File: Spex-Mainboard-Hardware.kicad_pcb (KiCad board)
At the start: 4 copper layers, 100 x 80 mm, 141 parts, among them K1 G5LE_1A4_DC3, K2 G5LE_1A4_DC3, P1 USB_OTG, P10 CONN_01X02, P11 CONN_01X02, P12 CONN_01X02, P2 SWD Header, P3 CONN_01X04, P4 CONN_01X04, P5 CONN_01X04, P6 CONN_01X04, P7 CONN_01X02, P8 CONN_01X02, P9 CONN_01X02, Q1 2N7002K, Q101 MOS_N_numbered, Q104 MOS_N_numbered, Q105 Si3407DV, Q106 Q_PNP_BEC, Q2 2N7002K, Q3 BSS215PH6327, Q4 Si5468DC, Q5 Si5468DC, Q6 Si5468DC, SW1 SW_PUSH, U1 MKL04Z32VLC4, U10 LM4030, U105 TPS563200, U108 TPS563200, U11 MCP2551-I/SN, U12 ST1480ABDR, U13 SCHA4B0419, U14 AT45DB641E, U2 NUP2201MR6, U3 MK20DX256VLH7, U4 NUP2201MR6, U5 NUP2201MR6, U6 MMQA6V2T1G, U7 MCP9808T, U8 BME280, U9 LSM9DS1, Y1 Crystal

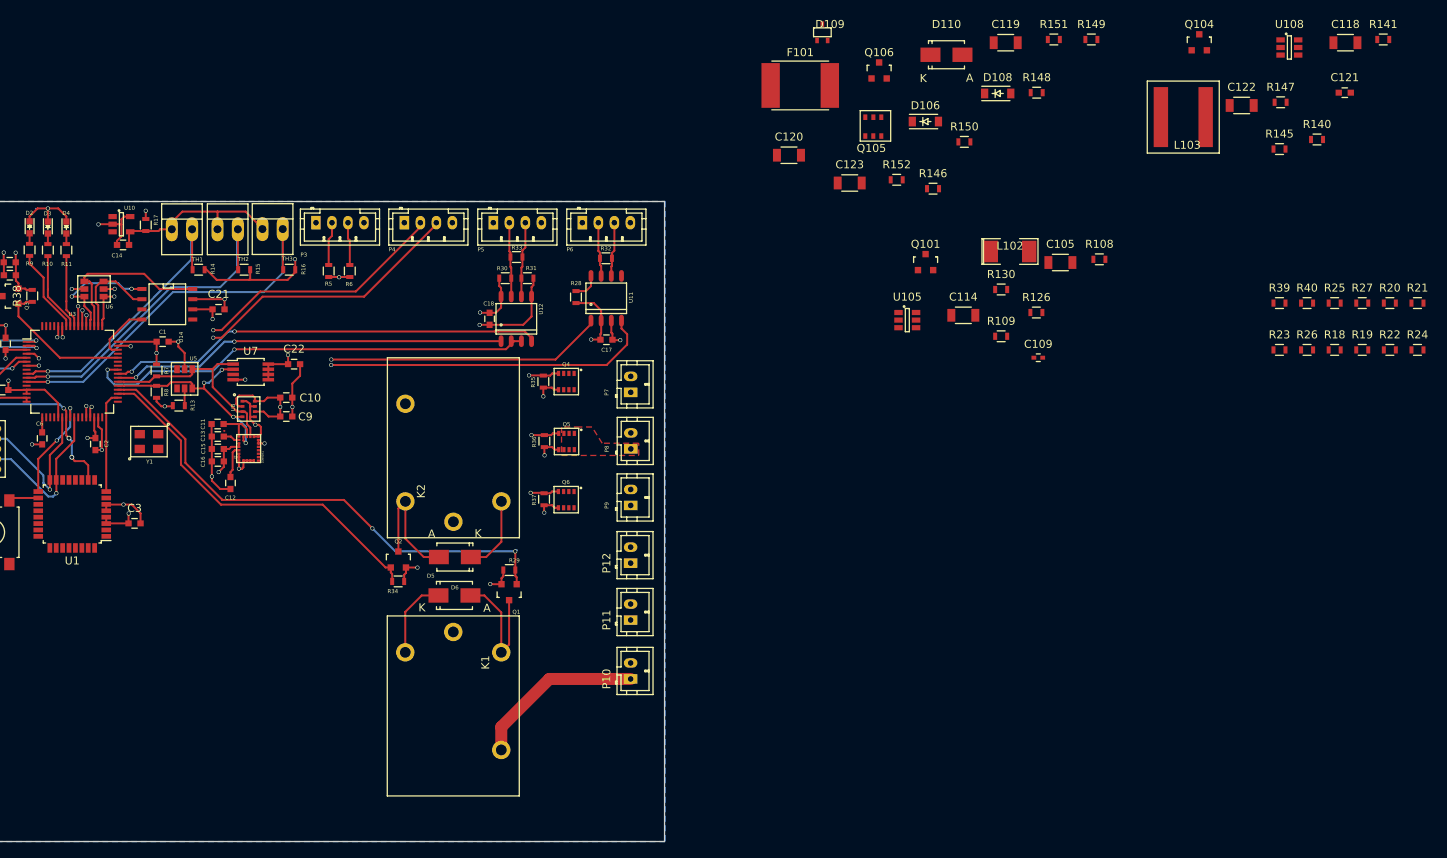
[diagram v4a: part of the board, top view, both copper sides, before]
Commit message: Added powerz
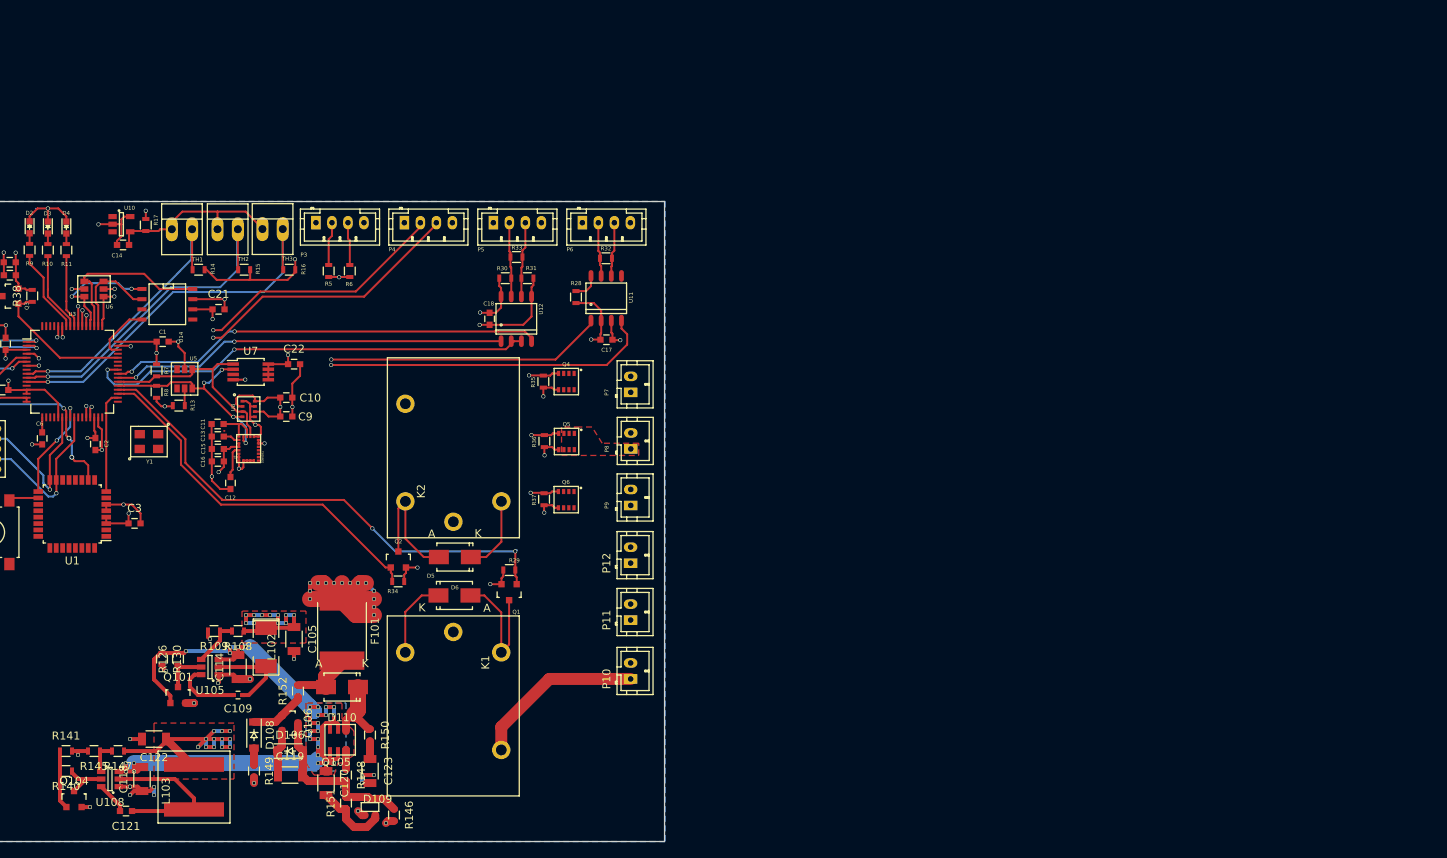
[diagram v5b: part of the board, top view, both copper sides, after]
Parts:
- removed R18, R19, R20, R21, R22, R23, R24, R25, R26, R27, R39, R40: R, Resistors_SMD:R_0603
- moved R141 187.1 mm to (109.0, 119.5)
- moved C121 176.8 mm to (116.5, 127.0), turned to 180 degrees
- moved C118 176.4 mm to (118.5, 123.0), turned to 90 degrees
- moved R140 175.2 mm to (109.0, 122.0), turned to 180 degrees
- moved U108 173.5 mm to (114.5, 123.0), turned to 180 degrees
- moved Q104 169.5 mm to (110.0, 125.5)
- moved R147 166.4 mm to (115.5, 119.5), turned to 180 degrees
- moved R145 166.2 mm to (112.5, 119.5), turned to 180 degrees
- moved C122 157.3 mm to (120.0, 118.0), turned to 180 degrees
- moved L103 149.3 mm to (125.0, 124.0), turned to 270 degrees
- moved R149 139.0 mm to (132.5, 122.0), turned to 270 degrees
- moved R151 130.1 mm to (144.0, 126.0), turned to 90 degrees
- moved C119 128.0 mm to (137.0, 122.5)
- moved D108 122.8 mm to (132.5, 117.5), turned to 270 degrees
- moved R148 121.4 mm to (144.0, 122.5), turned to 270 degrees
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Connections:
- C105 pad 1: /Power Distribution/12Vto3v3.sch/Vout -> +3V3
- C122 pad 1: /Power Distribution/12Vto5V.sch/Vout -> +5V
- C123 pad 2: /Power Distribution/protection.sch/GND -> GND
- D109 pad 1: /Power Distribution/protection.sch/GND -> GND
- D110 pad 1: Net-(D110-Pad1) -> Net-(C119-Pad1)
- D110 pad 2: Net-(C119-Pad1) -> Net-(D110-Pad2)
- F101 pad 1: /Power Distribution/protection.sch/Vin -> VBatt
- F101 pad 2: Net-(D110-Pad1) -> Net-(D110-Pad2)
- L102 pad 1: /Power Distribution/12Vto3v3.sch/Vout -> +3V3
- L103 pad 1: /Power Distribution/12Vto5V.sch/Vout -> +5V
- P2 pad 10: /RESET_b -> (no net)
- P2 pad 6: Net-(P2-Pad6) -> (no net)
- P2 pad 7: Net-(P2-Pad7) -> (no net)
- P2 pad 8: Net-(P2-Pad8) -> (no net)
- P2 pad 9: Net-(P2-Pad9) -> (no net)
- P9 pad 2: Vbus -> (no net)
- Q3 pad 3: Net-(Q3-Pad3) -> (no net)
- R108 pad 1: /Power Distribution/12Vto3v3.sch/Vout -> +3V3
- R146 pad 2: /Power Distribution/protection.sch/GND -> GND
- R147 pad 1: /Power Distribution/12Vto5V.sch/Vout -> +5V
- R149 pad 2: /Power Distribution/protection.sch/GND -> GND
- R152 pad 2: Net-(D110-Pad1) -> Net-(D110-Pad2)
- U1 pad 1: Net-(U1-Pad1) -> (no net)
- U1 pad 11: Net-(U1-Pad11) -> (no net)
- U1 pad 12: Net-(U1-Pad12) -> (no net)
- U1 pad 13: Net-(U1-Pad13) -> (no net)
- U1 pad 14: Net-(U1-Pad14) -> (no net)
- U1 pad 19: Net-(U1-Pad19) -> (no net)
- U1 pad 2: Net-(U1-Pad2) -> (no net)
- U1 pad 20: Net-(U1-Pad20) -> (no net)
- U1 pad 21: Net-(U1-Pad21) -> (no net)
- U1 pad 22: Net-(U1-Pad22) -> (no net)
- U1 pad 23: Net-(U1-Pad23) -> (no net)
- U1 pad 24: Net-(U1-Pad24) -> (no net)
- U1 pad 25: /PTB5 -> (no net)
- U1 pad 26: Net-(U1-Pad26) -> (no net)
- U1 pad 27: Net-(U1-Pad27) -> (no net)
- U1 pad 28: Net-(U1-Pad28) -> (no net)
- U1 pad 29: Net-(U1-Pad29) -> (no net)
- U1 pad 30: Net-(U1-Pad30) -> (no net)
- U1 pad 31: Net-(U1-Pad31) -> (no net)
- U1 pad 32: Net-(U1-Pad32) -> (no net)
- U1 pad 7: Net-(U1-Pad7) -> (no net)
- U1 pad 9: Net-(U1-Pad9) -> (no net)
- U10 pad 1: Net-(U10-Pad1) -> (no net)
- U10 pad 3: Net-(U10-Pad3) -> (no net)
- U11 pad 5: Net-(U11-Pad5) -> (no net)
- U14 pad 3: Net-(U14-Pad3) -> (no net)
- U14 pad 5: Net-(U14-Pad5) -> (no net)
- U2 pad 3: Net-(U2-Pad3) -> (no net)
- U2 pad 4: Net-(U2-Pad4) -> (no net)
- U3 pad 12: Net-(U3-Pad12) -> (no net)
- U3 pad 18: Net-(U3-Pad18) -> (no net)
- U3 pad 19: Net-(U3-Pad19) -> (no net)
- U3 pad 20: Net-(U3-Pad20) -> (no net)
- U3 pad 26: Net-(U3-Pad26) -> (no net)
- U3 pad 27: Net-(U3-Pad27) -> (no net)
- U3 pad 42: Net-(U3-Pad42) -> (no net)
- U3 pad 43: Net-(U3-Pad43) -> (no net)
- U3 pad 45: SD_Detect -> (no net)
- U3 pad 61: Net-(U3-Pad61) -> (no net)
- U3 pad 62: Net-(U3-Pad62) -> (no net)
- U3 pad 63: Net-(U3-Pad63) -> (no net)
- U3 pad 64: Net-(U3-Pad64) -> (no net)
- U3 pad 8: Net-(U3-Pad8) -> (no net)
- U4 pad 3: Net-(U4-Pad3) -> (no net)
- U4 pad 4: Net-(U4-Pad4) -> (no net)
- U5 pad 3: Net-(U5-Pad3) -> (no net)
- U5 pad 4: Net-(U5-Pad4) -> (no net)
- U7 pad 3: /HAB Sensors/TempAlert -> (no net)
- U9 pad 10: Net-(U9-Pad10) -> (no net)
- U9 pad 11: Net-(U9-Pad11) -> (no net)
- U9 pad 12: Net-(U9-Pad12) -> (no net)
- U9 pad 13: Net-(U9-Pad13) -> (no net)
- U9 pad 9: Net-(U9-Pad9) -> (no net)
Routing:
- net GND: track 155.0 -> 271.3 mm, vias 28 -> 47
- net /Power Distribution/VBus: track 0.00 -> 105.7 mm, vias 0 -> 28
- net VBatt: track 0.00 -> 36.6 mm, vias 0 -> 14
- net +5V: track 0.00 -> 32.1 mm, vias 0 -> 12
- net Net-(C119-Pad2): track 0.00 -> 21.3 mm
- net Net-(C121-Pad1): track 0.00 -> 19.6 mm
- net +3V3: track 111.8 -> 129.7 mm, vias 18 -> 29
- net Net-(C119-Pad1): track 0.00 -> 15.3 mm
- net Net-(C109-Pad1): track 0.00 -> 11.2 mm
- net Net-(C120-Pad2): track 0.00 -> 9.42 mm
- net Net-(C109-Pad2): track 0.00 -> 8.49 mm
- net Net-(D110-Pad2): track 0.00 -> 7.73 mm
- net Net-(D108-Pad1): track 0.00 -> 6.97 mm
- net Net-(Q104-Pad3): track 0.00 -> 6.31 mm
- net Net-(R108-Pad2): track 0.00 -> 6.02 mm
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- added copper zone on F.Cu, net +3V3
- added copper zone on F.Cu, net +5V
- added copper zone on B.Cu, net /Power Distribution/VBus
- added copper zone on F.Cu, net /Power Distribution/VBus

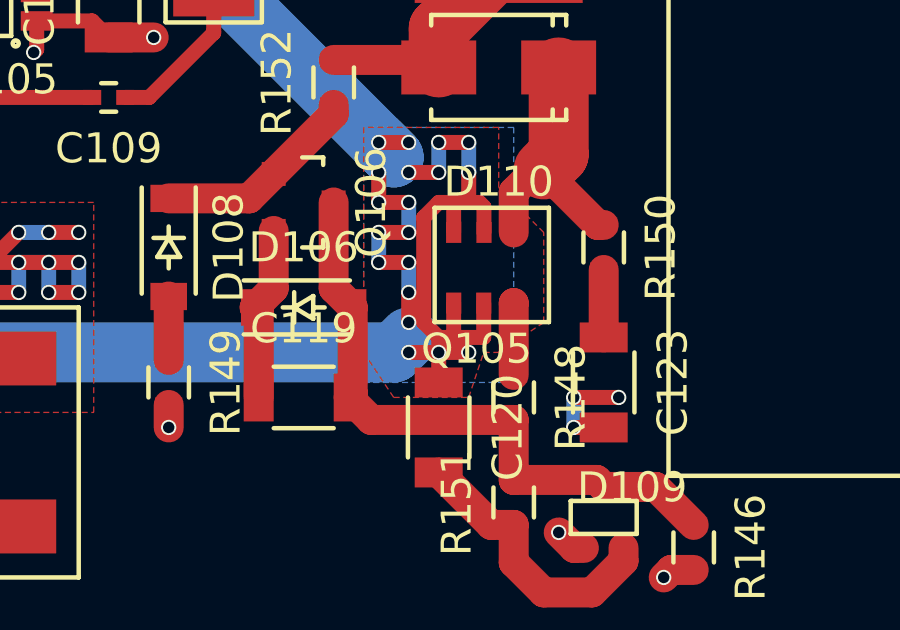
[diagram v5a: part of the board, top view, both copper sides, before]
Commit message: Routed a line.
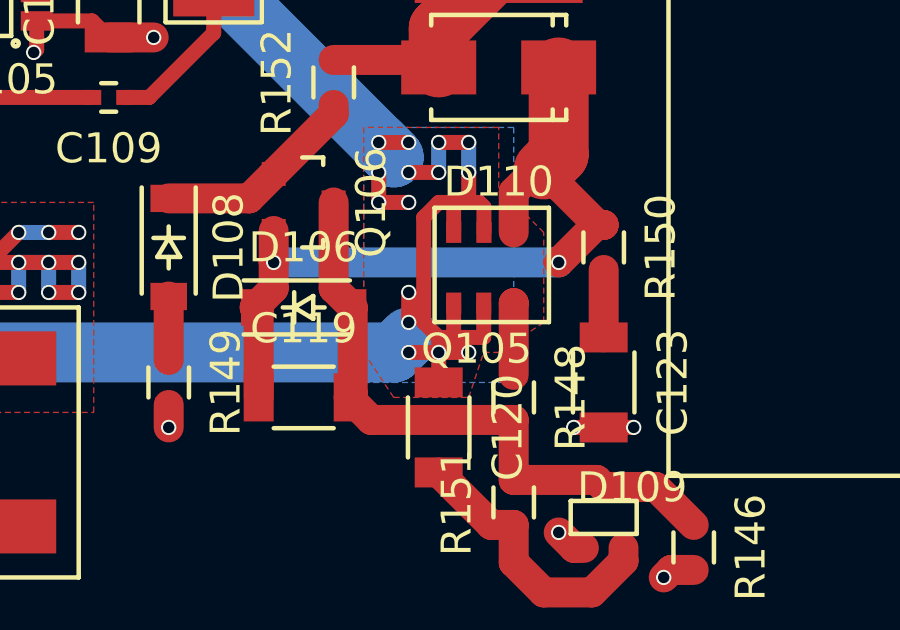
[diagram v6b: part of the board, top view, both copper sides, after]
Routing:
- net Net-(C119-Pad1): track 15.3 -> 26.8 mm, vias 0 -> 2
- net /Power Distribution/VBus: track 105.7 -> 103.7 mm, vias 28 -> 24
- net GND: track 271.3 -> 269.8 mm, vias 47 -> 46
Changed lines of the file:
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@@
     (links 339)
     (no_connects 96)
-    (area 83.744999 50.734999 183.895001 130.885001)
+    (area 61.191199 50.64563 184.6705 130.885001)
     (thickness 1.6)
     (drawings 4)
-    (tracks 1203)
+    (tracks 1199)
     (zones 0)
     (modules 129)
@@
   )
   (setup
-    (last_trace_width 0.5)
+    (last_trace_width 1)
     (user_trace_width 0.5)
     (user_trace_width 1)
@@
   (segment (start 115.4788 68.3352) (end 120.3226 68.3352) (width 0.25) (layer F.Cu) (net 1))
   (segment (start 120.3226 68.3352) (end 120.3318 68.326) (width 0.25) (layer F.Cu) (net 1))
+  (segment (start 147 123.5) (end 148 123.5) (width 0.5) (layer F.Cu) (net 2))
+  (via (at 148 123.5) (size 0.508) (drill 0.381) (layers F.Cu B.Cu) (net 2))
   (segment (start 145.5 127) (end 136 127) (width 0.5) (layer In1.Cu) (net 2))
   (segment (start 136 127) (end 132.5 123.5) (width 0.5) (layer In1.Cu) (net 2))
@@
   (segment (start 149 128.5) (end 147 128.5) (width 0.5) (layer In1.Cu) (net 2))
   (segment (start 147 128.5) (end 145.5 127) (width 0.5) (layer In1.Cu) (net 2))
-  (segment (start 146 122.5) (end 147.5 122.5) (width 0.5) (layer F.Cu) (net 2))
-  (via (at 147.5 122.5) (size 0.508) (drill 0.381) (layers F.Cu B.Cu) (net 2))
-  (segment (start 146 123.5) (end 146 122.5) (width 0.5) (layer B.Cu) (net 2))
-  (via (at 146 122.5) (size 0.508) (drill 0.381) (layers F.Cu B.Cu) (net 2))
   (segment (start 147 123.5) (end 146 123.5) (width 0.5) (layer F.Cu) (net 2))
   (via (at 146 123.5) (size 0.508) (drill 0.381) (layers F.Cu B.Cu) (net 2))
@@
   (segment (start 125.05 109.95) (end 124.5 110.5) (width 0.5) (layer F.Cu) (net 58))
   (segment (start 125.9 109.95) (end 125.05 109.95) (width 0.5) (layer F.Cu) (net 58))
+  (segment (start 135.99924 116.95) (end 135.99924 118) (width 1) (layer F.Cu) (net 59))
+  (segment (start 135.99924 118) (end 135.99924 118.86576) (width 1) (layer F.Cu) (net 59))
+  (segment (start 145.5 118) (end 135.99924 118) (width 1) (layer B.Cu) (net 59))
+  (via (at 135.99924 118) (size 0.508) (drill 0.381) (layers F.Cu B.Cu) (net 59))
+  (segment (start 147 116.75) (end 146.75 116.75) (width 1) (layer F.Cu) (net 59))
+  (segment (start 146.75 116.75) (end 145.5 118) (width 1) (layer F.Cu) (net 59))
+  (via (at 145.5 118) (size 0.508) (drill 0.381) (layers F.Cu B.Cu) (net 59))
   (segment (start 135.5 122.5) (end 135.5 119.635) (width 1) (layer F.Cu) (net 59))
   (segment (start 135.5 119.635) (end 135.365 119.5) (width 1) (layer F.Cu) (net 59))
-  (segment (start 135.99924 116.95) (end 135.99924 118.86576) (width 1) (layer F.Cu) (net 59))
   (segment (start 135.99924 118.86576) (end 135.365 119.5) (width 1) (layer F.Cu) (net 59))
   (segment (start 147 116.75) (end 146.8 116.75) (width 1) (layer F.Cu) (net 59))
@@
   (segment (start 113.25 121.9) (end 113.4 122.05) (width 0.5) (layer F.Cu) (net 71))
   (segment (start 113.25 119.5) (end 114.75 119.5) (width 0.5) (layer F.Cu) (net 71))
+  (segment (start 140.5 119) (end 140.5 116) (width 1) (layer In1.Cu) (net 72))
   (segment (start 123 107.25) (end 123.75 107.25) (width 0.5) (layer F.Cu) (net 72))
   (segment (start 123.75 107.25) (end 124 107) (width 0.5) (layer F.Cu) (net 72))
@@
   (segment (start 140.5 119) (end 140.5 120) (width 0.5) (layer F.Cu) (net 72))
   (via (at 140.5 120) (size 0.508) (drill 0.381) (layers F.Cu B.Cu) (net 72))
-  (segment (start 140.5 118) (end 140.5 119) (width 0.5) (layer B.Cu) (net 72))
   (via (at 140.5 119) (size 0.508) (drill 0.381) (layers F.Cu B.Cu) (net 72))
-  (segment (start 139.5 118) (end 140.5 118) (width 0.5) (layer F.Cu) (net 72))
-  (via (at 140.5 118) (size 0.508) (drill 0.381) (layers F.Cu B.Cu) (net 72))
-  (segment (start 139.5 117) (end 139.5 118) (width 0.5) (layer B.Cu) (net 72))
-  (via (at 139.5 118) (size 0.508) (drill 0.381) (layers F.Cu B.Cu) (net 72))
-  (segment (start 140.5 117) (end 139.5 117) (width 0.5) (layer F.Cu) (net 72))
-  (via (at 139.5 117) (size 0.508) (drill 0.381) (layers F.Cu B.Cu) (net 72))
-  (segment (start 140.5 116) (end 140.5 117) (width 0.5) (layer B.Cu) (net 72))
-  (via (at 140.5 117) (size 0.508) (drill 0.381) (layers F.Cu B.Cu) (net 72))
   (segment (start 139.5 116) (end 140.5 116) (width 0.5) (layer F.Cu) (net 72))
   (via (at 140.5 116) (size 0.508) (drill 0.381) (layers F.Cu B.Cu) (net 72))
@@
     (connect_pads (clearance 0.508))
     (min_thickness 0.254)
-    (fill (arc_segments 16) (thermal_gap 1.016) (thermal_bridge_width 0.508))
+    (fill yes (arc_segments 16) (thermal_gap 1.016) (thermal_bridge_width 0.508))
     (polygon
       (pts
@@
     (connect_pads (clearance 0.508))
     (min_thickness 0.254)
-    (fill (arc_segments 16) (thermal_gap 1.016) (thermal_bridge_width 0.508))
+    (fill yes (arc_segments 16) (thermal_gap 1.016) (thermal_bridge_width 0.508))
     (polygon
       (pts
@@
     (connect_pads (clearance 0.508))
     (min_thickness 0.254)
-    (fill (arc_segments 16) (thermal_gap 1.016) (thermal_bridge_width 0.508))
+    (fill yes (arc_segments 16) (thermal_gap 1.016) (thermal_bridge_width 0.508))
     (polygon
       (pts
@@
     (connect_pads (clearance 0.1))
     (min_thickness 0.254)
-    (fill (arc_segments 16) (thermal_gap 1.016) (thermal_bridge_width 0.508))
+    (fill yes (arc_segments 16) (thermal_gap 1.016) (thermal_bridge_width 0.508))
     (polygon
       (pts
@@
     (connect_pads (clearance 0.1))
     (min_thickness 0.254)
-    (fill (arc_segments 16) (thermal_gap 0.508) (thermal_bridge_width 0.508))
+    (fill yes (arc_segments 16) (thermal_gap 0.508) (thermal_bridge_width 0.508))
     (polygon
       (pts
@@
     (connect_pads (clearance 0.1))
     (min_thickness 0.254)
-    (fill (arc_segments 16) (thermal_gap 0.508) (thermal_bridge_width 0.508))
+    (fill yes (arc_segments 16) (thermal_gap 0.508) (thermal_bridge_width 0.508))
     (polygon
       (pts
@@
     (connect_pads (clearance 0.1))
     (min_thickness 0.254)
-    (fill (arc_segments 16) (thermal_gap 0.508) (thermal_bridge_width 0.508))
+    (fill yes (arc_segments 16) (thermal_gap 0.508) (thermal_bridge_width 0.508))
     (polygon
       (pts
@@
     (min_thickness 0.254)
     (keepout (tracks allowed) (vias allowed) (copperpour not_allowed))
-    (fill (arc_segments 16) (thermal_gap 0.508) (thermal_bridge_width 0.508))
+    (fill yes (arc_segments 16) (thermal_gap 0.508) (thermal_bridge_width 0.508))
     (polygon
       (pts
@@
     (connect_pads (clearance 0.1))
     (min_thickness 0.254)
-    (fill (arc_segments 16) (thermal_gap 0.508) (thermal_bridge_width 0.508))
+    (fill yes (arc_segments 16) (thermal_gap 0.508) (thermal_bridge_width 0.508))
     (polygon
       (pts
@@
     (min_thickness 0.254)
     (keepout (tracks allowed) (vias allowed) (copperpour not_allowed))
-    (fill (arc_segments 16) (thermal_gap 0.508) (thermal_bridge_width 0.508))
+    (fill yes (arc_segments 16) (thermal_gap 0.508) (thermal_bridge_width 0.508))
     (polygon
       (pts
@@
     (connect_pads (clearance 0.1))
     (min_thickness 0.254)
-    (fill (arc_segments 16) (thermal_gap 0.508) (thermal_bridge_width 0.508))
+    (fill yes (arc_segments 16) (thermal_gap 0.508) (thermal_bridge_width 0.508))
     (polygon
       (pts
@@
     (connect_pads (clearance 0.1))
     (min_thickness 0.254)
-    (fill (arc_segments 16) (thermal_gap 0.508) (thermal_bridge_width 1))
+    (fill yes (arc_segments 16) (thermal_gap 0.508) (thermal_bridge_width 1))
     (polygon
       (pts
@@
     (connect_pads (clearance 0.1))
     (min_thickness 0.254)
-    (fill (arc_segments 16) (thermal_gap 0.508) (thermal_bridge_width 1))
+    (fill yes (arc_segments 16) (thermal_gap 0.508) (thermal_bridge_width 1))
     (polygon
       (pts
@@
     (min_thickness 0.254)
     (keepout (tracks allowed) (vias allowed) (copperpour not_allowed))
-    (fill (arc_segments 16) (thermal_gap 0.508) (thermal_bridge_width 0.508))
+    (fill yes (arc_segments 16) (thermal_gap 0.508) (thermal_bridge_width 0.508))
     (polygon
       (pts
@@
     (min_thickness 0.254)
     (keepout (tracks allowed) (vias allowed) (copperpour not_allowed))
-    (fill (arc_segments 16) (thermal_gap 0.508) (thermal_bridge_width 0.508))
+    (fill yes (arc_segments 16) (thermal_gap 0.508) (thermal_bridge_width 0.508))
     (polygon
       (pts
@@
     (min_thickness 0.254)
     (keepout (tracks allowed) (vias allowed) (copperpour not_allowed))
-    (fill (arc_segments 16) (thermal_gap 0.508) (thermal_bridge_width 0.508))
+    (fill yes (arc_segments 16) (thermal_gap 0.508) (thermal_bridge_width 0.508))
     (polygon
       (pts
@@
     (min_thickness 0.254)
     (keepout (tracks allowed) (vias allowed) (copperpour not_allowed))
-    (fill (arc_segments 16) (thermal_gap 0.508) (thermal_bridge_width 0.508))
+    (fill yes (arc_segments 16) (thermal_gap 0.508) (thermal_bridge_width 0.508))
     (polygon
       (pts
